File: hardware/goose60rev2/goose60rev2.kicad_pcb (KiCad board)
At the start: 2 copper layers, 285 x 95.1 mm, 211 parts, among them J1 USB_C_Receptacle_USB2.0_14P, J2 Conn_01x04_Pin, J3 Conn_01x04_Socket, J4 Conn_01x14_Socket, SW1 SW_Push, SW1_1 SW_Push, SW1_10 SW_Push, SW1_11 SW_Push, SW1_12 SW_Push, SW1_13 SW_Push, SW1_14 SW_Push, SW1_15 SW_Push, SW1_2 SW_Push, SW1_3 SW_Push, SW1_4 SW_Push, SW1_5 SW_Push, SW1_6 SW_Push, SW1_7 SW_Push, SW1_8 SW_Push, SW1_9 SW_Push, SW2_1 SW_Push, SW2_10 SW_Push, SW2_11 SW_Push, SW2_12 SW_Push, SW2_13 SW_Push, SW2_14 SW_Push, SW2_2 SW_Push, SW2_3 SW_Push, SW2_4 SW_Push, SW2_5 SW_Push, SW2_6 SW_Push, SW2_7 SW_Push, SW2_8 SW_Push, SW2_9 SW_Push, SW3_1 SW_Push, SW3_10 SW_Push, SW3_11 SW_Push, SW3_12 SW_Push, SW3_13 SW_Push, SW3_14 SW_Push, SW3_2 SW_Push, SW3_3 SW_Push, SW3_4 SW_Push, SW3_5 SW_Push, SW3_6 SW_Push, SW3_7 SW_Push, SW3_8 SW_Push, SW3_9 SW_Push, SW4_1 SW_Push, SW4_10 SW_Push, SW4_11 SW_Push, SW4_12 SW_Push, SW4_13 SW_Push, SW4_14 SW_Push, SW4_15 SW_Push, SW4_3 SW_Push, SW4_4 SW_Push, SW4_5 SW_Push, SW4_6 SW_Push, SW4_7 SW_Push, SW4_8 SW_Push, SW4_9 SW_Push, SW5_1 SW_Push, SW5_10 SW_Push, SW5_11 SW_Push, SW5_12 SW_Push, SW5_13 SW_Push, SW5_14 SW_Push, SW5_15 SW_Push, SW5_16 SW_Push, SW5_17 SW_Push, SW5_18 SW_Push, SW5_2 SW_Push, SW5_3 SW_Push, SW5_4 SW_Push, SW5_5 SW_Push, SW5_6 SW_Push, SW5_7 SW_Push, SW5_8 SW_Push, SW5_9 SW_Push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

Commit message: update rev2 pcb layout
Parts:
- moved C17 2.83 mm to (184.0, 187.6), turned to 0 degrees
- moved R14 1.95 mm to (180.1, 186.6), turned to -90 degrees
- moved C16 1.94 mm to (180.1, 183.0), turned to 90 degrees
- moved X1 1.35 mm to (183.2, 184.6)
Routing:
- net GND: track 550.2 -> 539.5 mm, vias 721 -> 718
- net XR: track 3.66 -> 6.08 mm
- net XOUT: track 7.52 -> 5.52 mm

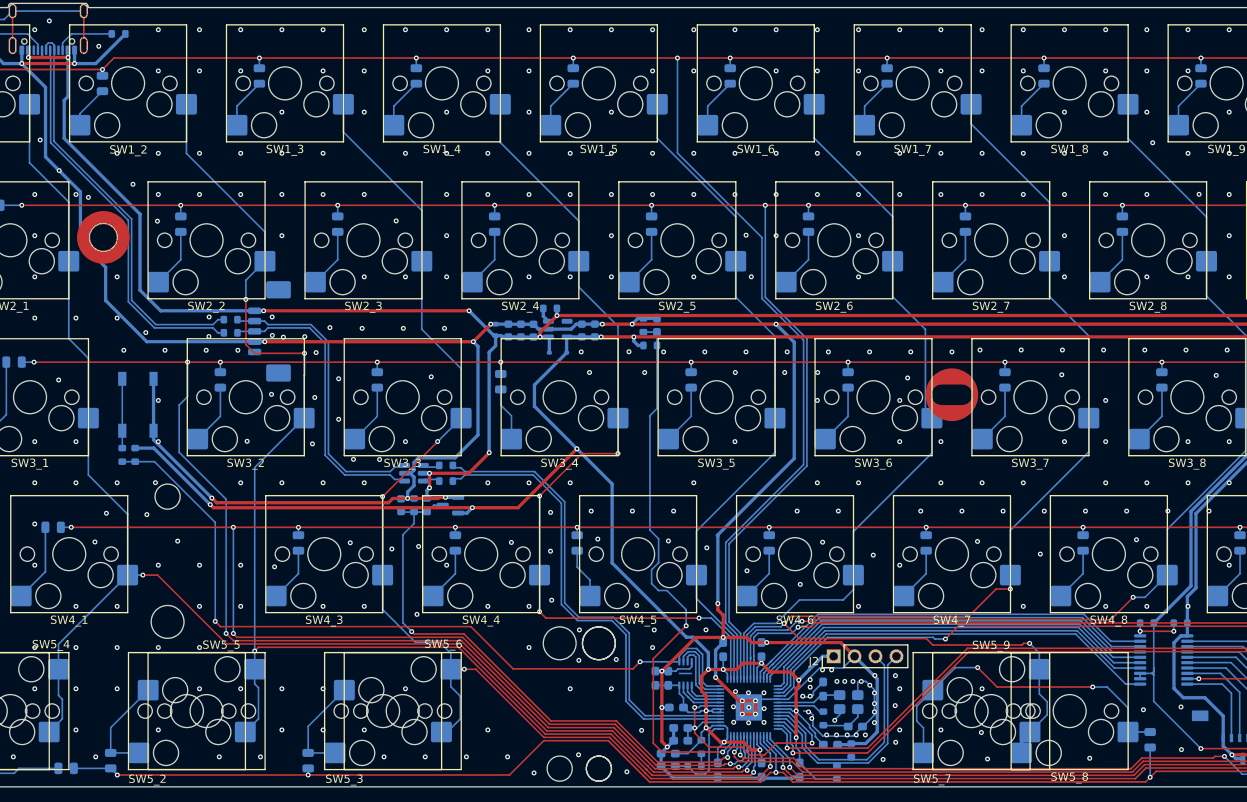
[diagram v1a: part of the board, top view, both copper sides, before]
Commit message: feat(pcb): enable teardrops and fine-tune via layout
- Enable teardrops on pads, vias, and THT footprints for enhanced mechanical reliability
- Fine-tune R12 placement and align GND vias
- Update connector schematic bus aliases
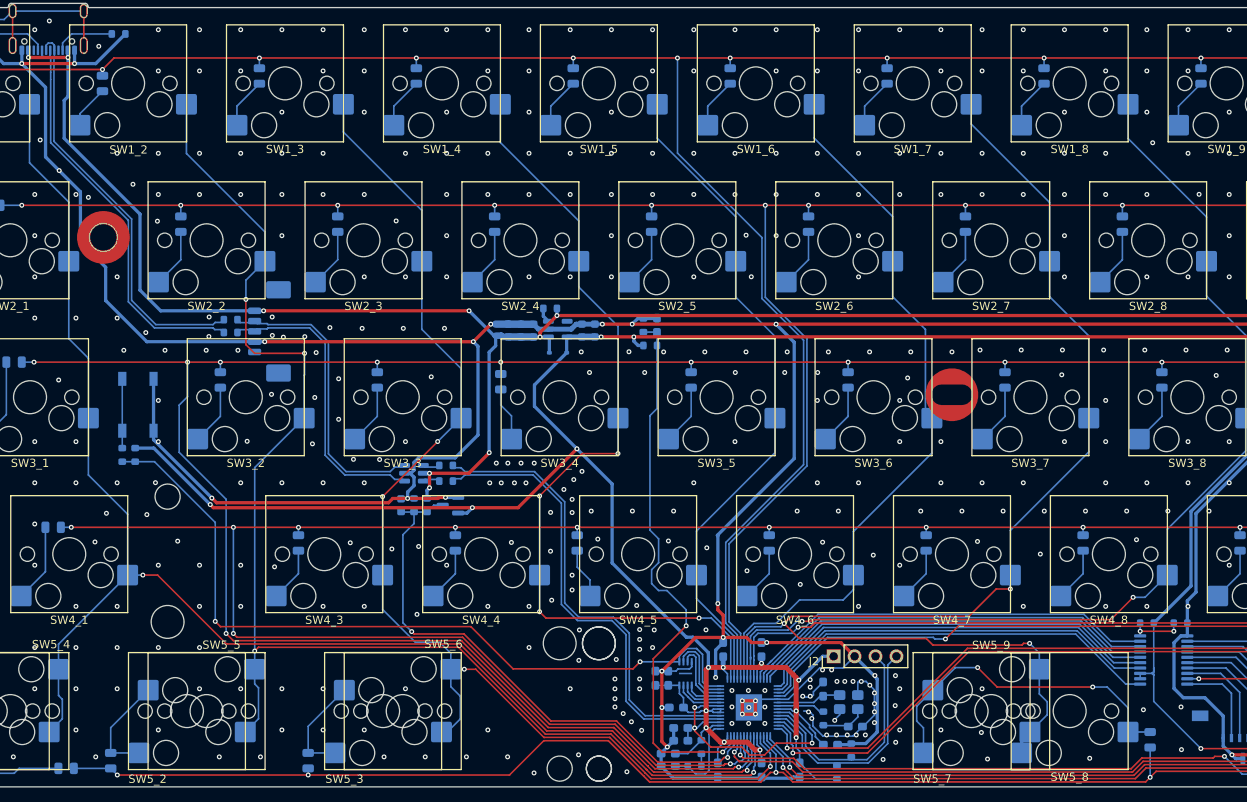
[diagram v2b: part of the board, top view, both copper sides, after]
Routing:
- net GND: track 539.5 -> 535.1 mm, vias 718 -> 740
- net +3.3V: track 375.1 -> 377.1 mm
